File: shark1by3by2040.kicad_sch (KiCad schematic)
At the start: 23 parts, among them U1 RP2040

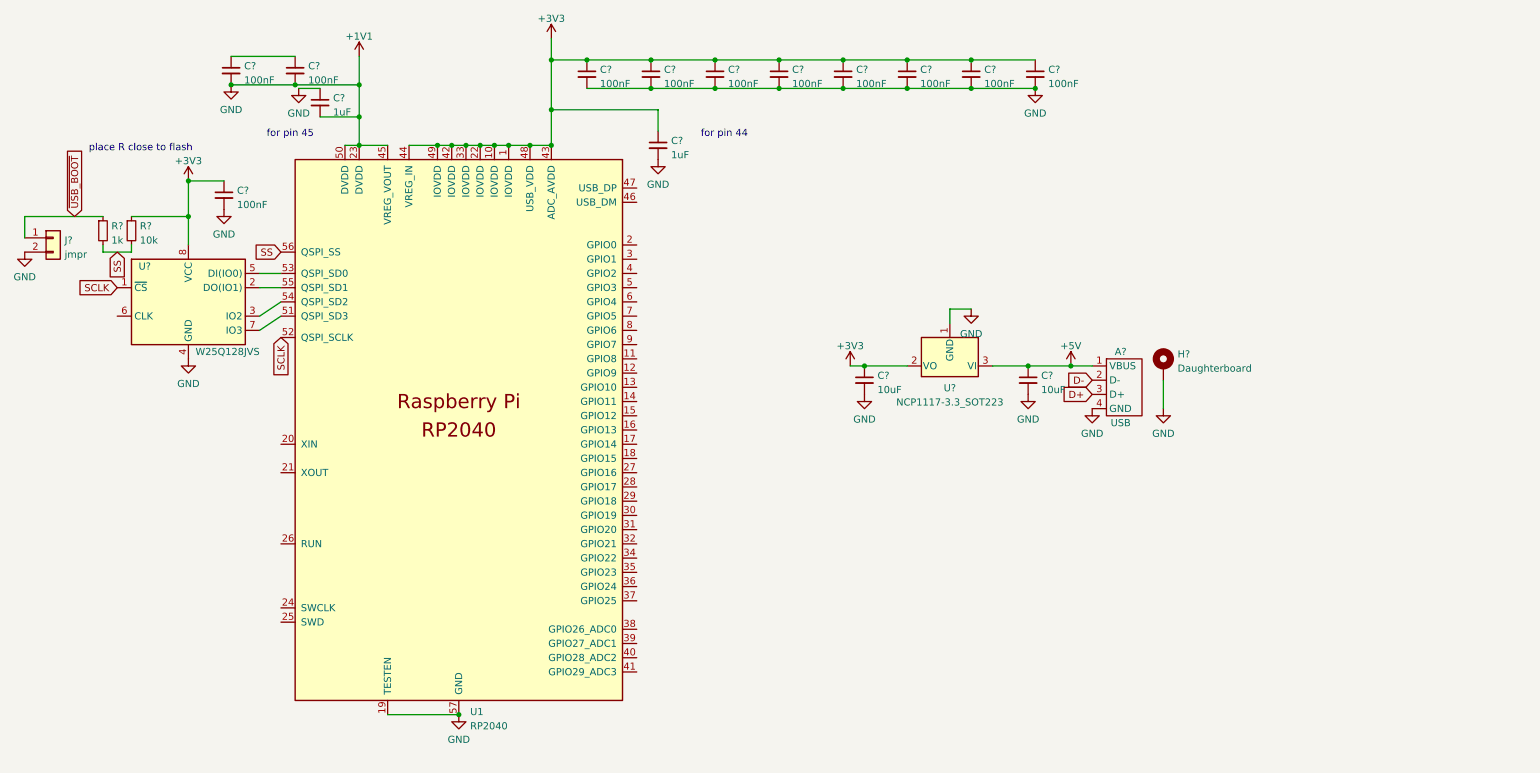
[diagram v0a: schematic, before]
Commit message: basic working rp2040
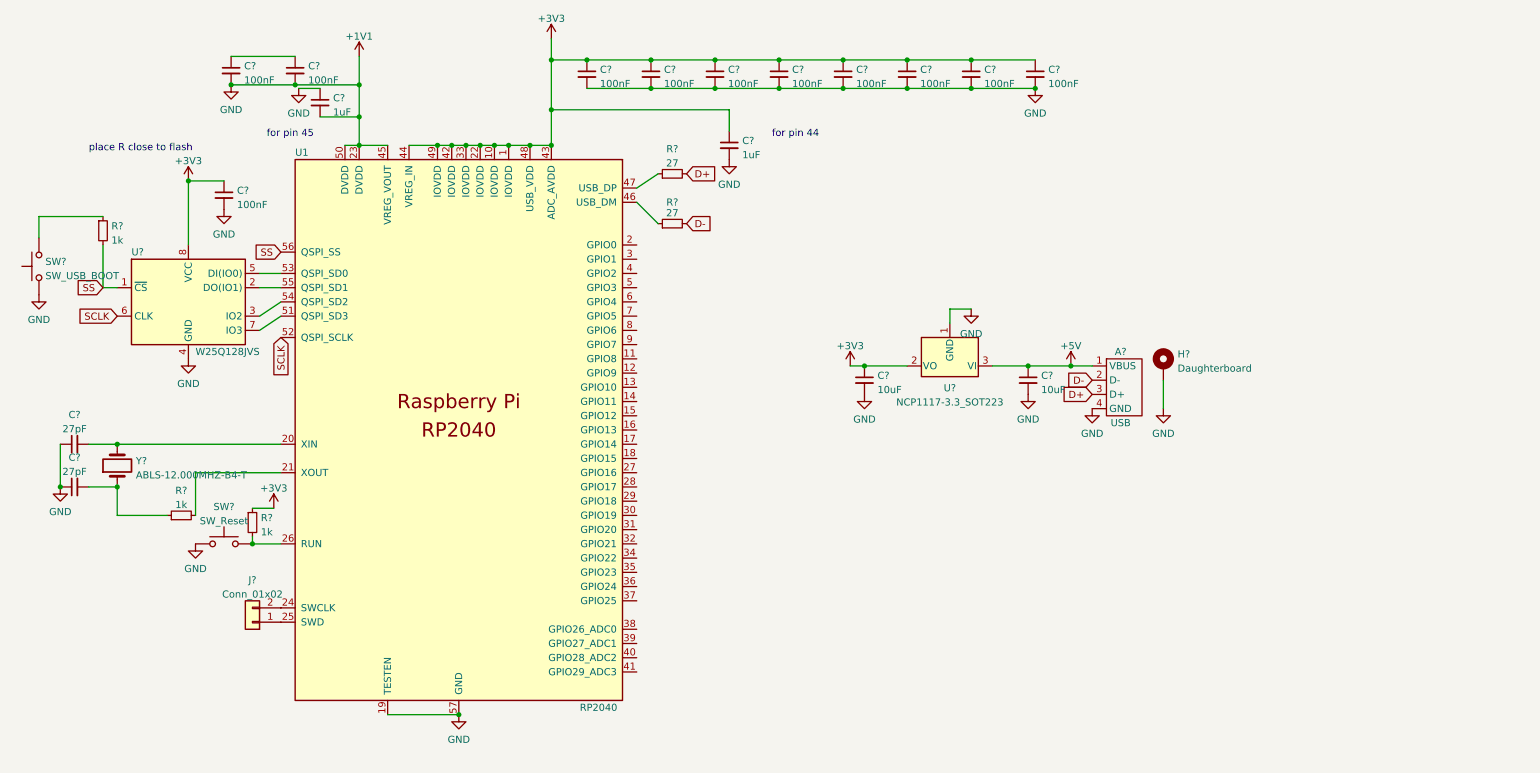
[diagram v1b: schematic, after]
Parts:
- removed J?: jmpr, symbol Connector_Generic:Conn_01x02
- removed R?: 10k, symbol Device:R_Small
- added C? (x2): 27pF, symbol Device:C_Small
- added J?: Conn_01x02, symbol Connector_Generic:Conn_01x02
- added R? (x2): 1k, symbol Device:R_Small
- added R? (x2): 27, symbol Device:R_Small
- added SW?: SW_Reset, symbol Switch:SW_Push
- added SW?: SW_USB_BOOT, symbol Switch:SW_Push
- added Y?: ABLS-12.000MHZ-B4-T, symbol Device:Crystal
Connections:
- net +1V1: now also C?.1, C?.1, SW?.1, SW?.1
- net +3V3: now also R?.1
- net D+: now also R?.2
- net D-: now also R?.2
- net SCLK: now also U?.6 (CLK); no longer U?.1 (~{CS})
- net SS: now also U?.1 (~{CS})
- net at U1.20 (XIN): now also C?.2, Y?.2
- net at U1.21 (XOUT): now also R?.2
- net at U1.24 (SWCLK): now also J?.2 (Pin_2)
- net at U1.25 (SWD): now also J?.1 (Pin_1)
- net at U1.26 (RUN): now also R?.2, SW?.2
- net at U1.46 (USB_DM): now also R?.1
- net at U1.47 (USB_DP): now also R?.1
- net ~{USB_BOOT}: no longer names the net of R?.1
- net ~{USB_BOOT}: now also SW?.2
- new net: C?.2, R?.1, Y?.1
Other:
- moved on the sheet: C?

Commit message: make 1by3, do most of work on pcb
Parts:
- removed C? (x2): 100nF, symbol Device:C_Small
- removed J?: Conn_01x02, symbol Connector_Generic:Conn_01x02
- added D1, D2, D3: D_Small, Diode_SMD:D_SOD-123, symbol Device:D_Small
- added J1: SWD, Connector_PinHeader_2.54mm:PinHeader_1x04_P2.54mm_Vertical, symbol Connector_Generic:Conn_01x04
- added MX1: Z, marbastlib-mx:SW_MX_HS_1u, symbol marbastlib-mx:MX_SW_HS
- added MX2: X, marbastlib-mx:SW_MX_HS_1u, symbol marbastlib-mx:MX_SW_HS
- added MX3: C, marbastlib-mx:SW_MX_HS_1u, symbol marbastlib-mx:MX_SW_HS
- C1, C10, C11, C12, C13, C14, C15, C16, C17, C2, C3, C4, C5, C6, C7: renamed from C?; footprint (none) -> Capacitor_SMD:C_0805_2012Metric
- R1, R2, R3, R4, R5: renamed from R?; footprint (none) -> Resistor_SMD:R_0805_2012Metric
- SW1, SW2: renamed from SW?; footprint (none) -> local:TS-1187A
- Y1: renamed from Y?; footprint (none) -> Crystal:Crystal_SMD_HC49-SD
- gave numbers to parts that had none: 4
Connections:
- net +1V1: no longer A1.4 (GND), C10.2, C11.1, C12.2, C13.2, C14.2, C15.2, C16.1, C17.1, C3.2, C4.2, C5.2, C6.2, C7.2, H1.1, SW1.1, SW2.1, U1.19 (TESTEN), U1.57 (GND), U2.4 (GND), U3.1 (GND)
- net +3V3: now also C14.2, J1.3 (Pin_3); no longer C14.1
- net +5V: now also C15.2; no longer C15.1
- net GND: now reaches C1.1, C2.1
- net GND: now also A1.4 (GND), C10.2, C11.1, C12.2, C13.2, C14.1, C15.1, C16.1, C17.1, C3.2, C4.2, C5.2, C6.2, C7.2, H1.1, SW1.1, SW2.1, U1.19 (TESTEN), U1.57 (GND), U2.4 (GND), U3.1 (GND), J1.4 (Pin_4)
- net at U1.25 (SWD): now also J1.2 (Pin_2)
- net at U1.24 (SWCLK): now also J1.1 (Pin_1)
- net row0: now reaches U1.4 (GPIO2)
- net row0: now also D1.1 (K), D2.1 (K), D3.1 (K)
- net DN: now reaches R2.1, U1.46 (USB_DM)
- net DP: now reaches R1.1, U1.47 (USB_DP)
- net col2: now reaches U1.5 (GPIO3)
- net col2: now also MX3.1
- net col1: now reaches U1.6 (GPIO4)
- net col1: now also MX2.1
- net col0: now reaches U1.7 (GPIO5)
- net col0: now also MX1.1
- new net: D3.2 (A), MX3.2
- new net: D1.2 (A), MX1.2
- new net: D2.2 (A), MX2.2
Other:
- moved on the sheet: A1, C1, C10, C11, C12, C13, C14, C15, C16, C17, C2, C3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

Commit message: 1by3by2040 rev1
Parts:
- removed J1: SWD, Connector_PinHeader_2.54mm:PinHeader_1x04_P2.54mm_Vertical, symbol Connector_Generic:Conn_01x04
- SW1: value SW_USB_BOOT -> BOOTSEL
- SW2: value SW_Reset -> Reset
- U2: value W25Q128JVS -> W25Q16JVSSIQ
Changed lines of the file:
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@@
-    (stroke (width 0) (type default) (color 0 0 0 0))
-  )
-  (wire (pts (xy 60.96 123.19) (xy 62.23 123.19))
     (stroke (width 0) (type default) (color 0 0 0 0))
   )
@@
     (stroke (width 0) (type default) (color 0 0 0 0))
   )
-  (wire (pts (xy 60.96 120.65) (xy 62.23 120.65))
-    (stroke (width 0) (type default) (color 0 0 0 0))
-  )
   (wire (pts (xy 53.34 21.59) (xy 64.77 21.59))
     (stroke (width 0) (type default) (color 0 0 0 0))
@@
     (stroke (width 0) (type default) (color 0 0 0 0))
   )
-  (wire (pts (xy 62.23 125.73) (xy 60.96 125.73))
-    (stroke (width 0) (type default) (color 0 0 0 0))
-  )
   (wire (pts (xy 27.94 91.44) (xy 33.02 91.44))
     (stroke (width 0) (type default) (color 0 0 0 0))
@@
   )
   (wire (pts (xy 85.09 38.1) (xy 90.17 38.1))
-    (stroke (width 0) (type default) (color 0 0 0 0))
-  )
-  (wire (pts (xy 62.23 128.27) (xy 60.96 128.27))
     (stroke (width 0) (type default) (color 0 0 0 0))
   )
@@
     (pin "1")
     (pin "2")
-  )
-  (symbol (lib_id "Connector_Generic:Conn_01x04") (at 55.88 123.19 0) (mirror y) (unit 1)
-    (in_bom yes) (on_board yes) (fields_autoplaced)
-    (property "Reference" "J1" (id 0) (at 55.88 115.6802 0))
-    (property "Value" "SWD" (id 1) (at 55.88 118.2171 0))
-    (property "Footprint" "Connector_PinHeader_2.54mm:PinHeader_1x04_P2.54mm_Vertical" (id 2) (at 55.88 123.19 0)
-      (effects (font (size 1.27 1.27)) hide)
-    )
-    (property "Datasheet" "~" (id 3) (at 55.88 123.19 0)
-      (effects (font (size 1.27 1.27)) hide)
-    )
-    (pin "1")
-    (pin "2")
-    (pin "3")
-    (pin "4")
   )
   (symbol (lib_id "power:+3V3") (at 45.72 44.45 0) (unit 1)
@@
     (pin "2")
   )
-  (symbol (lib_id "power:GND") (at 62.23 128.27 90) (unit 1)
-    (in_bom yes) (on_board yes) (fields_autoplaced)
-    (property "Reference" "#PWR03" (id 0) (at 68.58 128.27 0)
-      (effects (font (size 1.27 1.27)) hide)
-    )
-    (property "Value" "GND" (id 1) (at 65.405 128.7038 90)
-      (effects (font (size 1.27 1.27)) (justify right))
-    )
-    (property "Footprint" "" (id 2) (at 62.23 128.27 0)
-      (effects (font (size 1.27 1.27)) hide)
-    )
-    (property "Datasheet" "" (id 3) (at 62.23 128.27 0)
-      (effects (font (size 1.27 1.27)) hide)
-    )
-    (pin "1")
-  )
   (symbol (lib_id "Device:C_Small") (at 173.99 25.4 0) (unit 1)
     (in_bom yes) (on_board yes) (fields_autoplaced)
@@
     (in_bom yes) (on_board yes) (fields_autoplaced)
     (property "Reference" "SW2" (id 0) (at 52.07 102.5992 0))
-    (property "Value" "SW_Reset" (id 1) (at 52.07 105.1361 0))
+    (property "Value" "Reset" (id 1) (at 52.07 105.1361 0))
     (property "Footprint" "local:TS-1187A" (id 2) (at 52.07 104.14 0)
       (effects (font (size 1.27 1.27)) hide)
@@
       (effects (font (size 1.27 1.27)) (justify left))
     )
-    (property "Value" "W25Q128JVS" (id 1) (at 46.99 74.93 0)
+    (property "Value" "W25Q16JVSSIQ" (id 1) (at 46.99 74.93 0)
       (effects (font (size 1.27 1.27)) (justify left))
     )
@@
     (pin "2")
   )
-  (symbol (lib_id "power:+3V3") (at 62.23 125.73 270) (unit 1)
-    (in_bom yes) (on_board yes) (fields_autoplaced)
-    (property "Reference" "#PWR02" (id 0) (at 58.42 125.73 0)
-      (effects (font (size 1.27 1.27)) hide)
-    )
-    (property "Value" "+3V3" (id 1) (at 65.405 126.1638 90)
-      (effects (font (size 1.27 1.27)) (justify left))
-    )
-    (property "Footprint" "" (id 2) (at 62.23 125.73 0)
-      (effects (font (size 1.27 1.27)) hide)
-    )
-    (property "Datasheet" "" (id 3) (at 62.23 125.73 0)
-      (effects (font (size 1.27 1.27)) hide)
-    )
-    (pin "1")
-  )
   (symbol (lib_id "Device:R_Small") (at 44.45 104.14 90) (unit 1)
     (in_bom yes) (on_board yes) (fields_autoplaced)
@@
       (effects (font (size 1.27 1.27)) (justify right))
     )
-    (property "Value" "SW_USB_BOOT" (id 1) (at 20.193 61.3922 90)
+    (property "Value" "BOOTSEL" (id 1) (at 20.193 61.3922 90)
       (effects (font (size 1.27 1.27)) (justify right))
     )
@@
       (reference "#PWR01") (unit 1) (value "GND") (footprint "")
     )
-    (path "/cae9f84e-5516-4cb2-9b19-5422e89bd94d"
-      (reference "#PWR02") (unit 1) (value "+3V3") (footprint "")
-    )
-    (path "/69a91000-bd39-44ad-a8e2-c9e7789fc8c7"
-      (reference "#PWR03") (unit 1) (value "GND") (footprint "")
-    )
     (path "/845ad9cc-e85a-44f5-ac32-7b5bbaf666b9"
       (reference "#PWR0101") (unit 1) (value "GND") (footprint "")
@@
       (reference "H1") (unit 1) (value "Daughterboard") (footprint "local:UNIFIED-DAUGHTERBOARD-C3")
     )
-    (path "/4c53c93a-d6b0-455e-b6e2-1ab941405582"
-      (reference "J1") (unit 1) (value "SWD") (footprint "Connector_PinHeader_2.54mm:PinHeader_1x04_P2.54mm_Vertical")
-    )
     (path "/f7c93a7e-6a6e-4bac-bc79-50e8954227c2"
       (reference "MX1") (unit 1) (value "Z") (footprint "marbastlib-mx:SW_MX_HS_1u")
@@
     )
     (path "/e4b9178d-3910-4768-9efe-cfbaa4c57e40"
-      (reference "SW1") (unit 1) (value "SW_USB_BOOT") (footprint "local:TS-1187A")
+      (reference "SW1") (unit 1) (value "BOOTSEL") (footprint "local:TS-1187A")
     )
     (path "/7ace4731-c4cf-4103-84ea-c78eae246ce9"
-      (reference "SW2") (unit 1) (value "SW_Reset") (footprint "local:TS-1187A")
+      (reference "SW2") (unit 1) (value "Reset") (footprint "local:TS-1187A")
     )
     (path "/51a5a484-74fe-49e7-ac0f-dc8fb58e6288"
@@
     )
     (path "/aac362b4-e05e-41be-898c-3e2afa50e165"
-      (reference "U2") (unit 1) (value "W25Q128JVS") (footprint "Package_SO:SOIC-8_5.23x5.23mm_P1.27mm")
+      (reference "U2") (unit 1) (value "W25Q16JVSSIQ") (footprint "Package_SO:SOIC-8_5.23x5.23mm_P1.27mm")
     )
     (path "/a5af56e1-ff80-4421-a2b6-0eb08dcd31e6"

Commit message: 1by3by2040 rev2
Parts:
- removed A1: USB, random-keyboard-parts:JST-SR-4, symbol local:UNIFIED-DAUGHTERBOARD-C3
- removed H1: Daughterboard, local:UNIFIED-DAUGHTERBOARD-C3, symbol Mechanical:MountingHole_Pad
- removed SW1: BOOTSEL, local:TS-1187A, symbol Switch:SW_Push
- removed SW2: Reset, local:TS-1187A, symbol Switch:SW_Push
- added F1: 500mA, Fuse:Fuse_0805_2012Metric, symbol Device:Polyfuse_Small
- added JP1: BOOTSEL, random-keyboard-parts:Jumper-UserFriendly-Small, symbol Jumper:SolderJumper_2_Open
- added U4: USBLC6-2SC6, Package_TO_SOT_SMD:SOT-23-6, symbol Power_Protection:USBLC6-2SC6
- added USB1: HRO-TYPE-C-31-M-12, Type-C:HRO-TYPE-C-31-M-12-Assembly, symbol Type-C:HRO-TYPE-C-31-M-12
- C1, C10, C11, C12, C13, C14, C15, C2, C3, C4, C5, C6, C7: footprint Capacitor_SMD:C_0805_2012Metric -> Capacitor_SMD:C_0402_1005Metric
- C16, C17: value 27pF -> 22pF; footprint Capacitor_SMD:C_0805_2012Metric -> Capacitor_SMD:C_0402_1005Metric
- D1, D2, D3: footprint Diode_SMD:D_SOD-123 -> random-keyboard-parts:D_SOD-123-Pretty
- R1, R2, R3: footprint Resistor_SMD:R_0805_2012Metric -> Resistor_SMD:R_0402_1005Metric
- R4, R5: value 1k -> 5.1k; footprint Resistor_SMD:R_0805_2012Metric -> Resistor_SMD:R_0402_1005Metric
- Y1: value ABLS-12.000MHZ-B4-T -> RH100-12.000-16-3030-TR; footprint Crystal:Crystal_SMD_HC49-SD -> Crystal:Crystal_SMD_3225-4Pin_3.2x2.5mm; symbol Device:Crystal -> Device:Crystal_GND24
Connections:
- net +3V3: now also U1.26 (RUN); no longer R5.1
- net +5V: now also F1.2, U4.5 (VBUS)
- net D+: now also U4.1 (I/O1)
- net D-: now also U4.3 (I/O2)
- net DN: now also U4.4 (I/O2), USB1.5 (DN2), USB1.7 (DN1); no longer R2.1, U1.46 (USB_DM)
- net DP: now also U4.6 (I/O1), USB1.6 (DP1), USB1.8 (DP2); no longer R1.1, U1.47 (USB_DP)
- net GND: now also C16.2, C17.2, R4.2, R5.2, Y1.2, Y1.4, JP1.1 (A), U4.2 (GND), USB1.1 (GND), USB1.12 (GND), USB1.13 (SHIELD); no longer C16.1, C17.1
- net XOUT: now reaches U1.21 (XOUT)
- net XOUT: now also C17.1, Y1.1; no longer R4.2
- net at R3.1: now also JP1.2 (B)
- new net: R2.1, U1.46 (USB_DM)
- new net: R1.1, U1.47 (USB_DP)
- new net: R5.1, USB1.10 (CC2)
- new net: R4.1, USB1.4 (CC1)
- new net VBUS: F1.1, USB1.11 (VBUS), USB1.2 (VBUS)
- new net XIN: C16.1, U1.20 (XIN), Y1.3
- no-connect marks 0 -> 2
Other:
- moved on the sheet: C14, C15, C16, C17, D1, D2, D3, MX1, MX2, MX3, U3
